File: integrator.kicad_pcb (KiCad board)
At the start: 4 copper layers, 65.5 x 117 mm, 97 parts, among them J1 SJ-3524-SMT, J2 SJ-3524-SMT, J5 USB4105-GF-A, J6 Conn_ARM_JTAG_SWD_10, J7 test point, SW1 EVQP40B3M, SW2 EVQP40B3M, SW3 EVQP40B3M, SW4 436333033816, U1 MCP1501T-30E_RW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

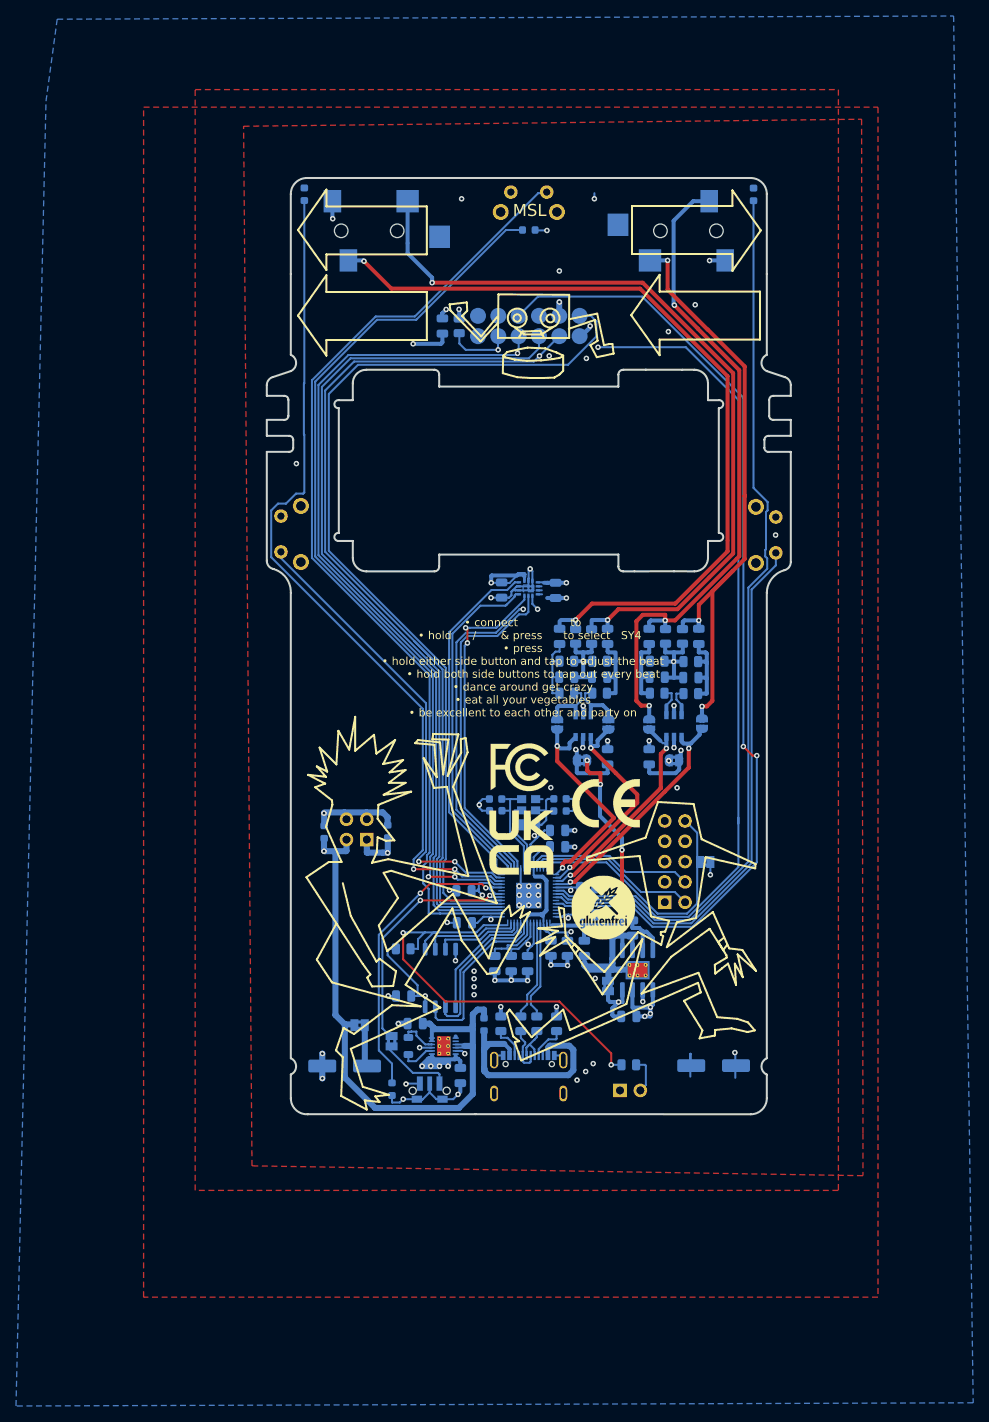
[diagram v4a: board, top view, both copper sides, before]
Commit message: adjusted jack positions, added back jumper
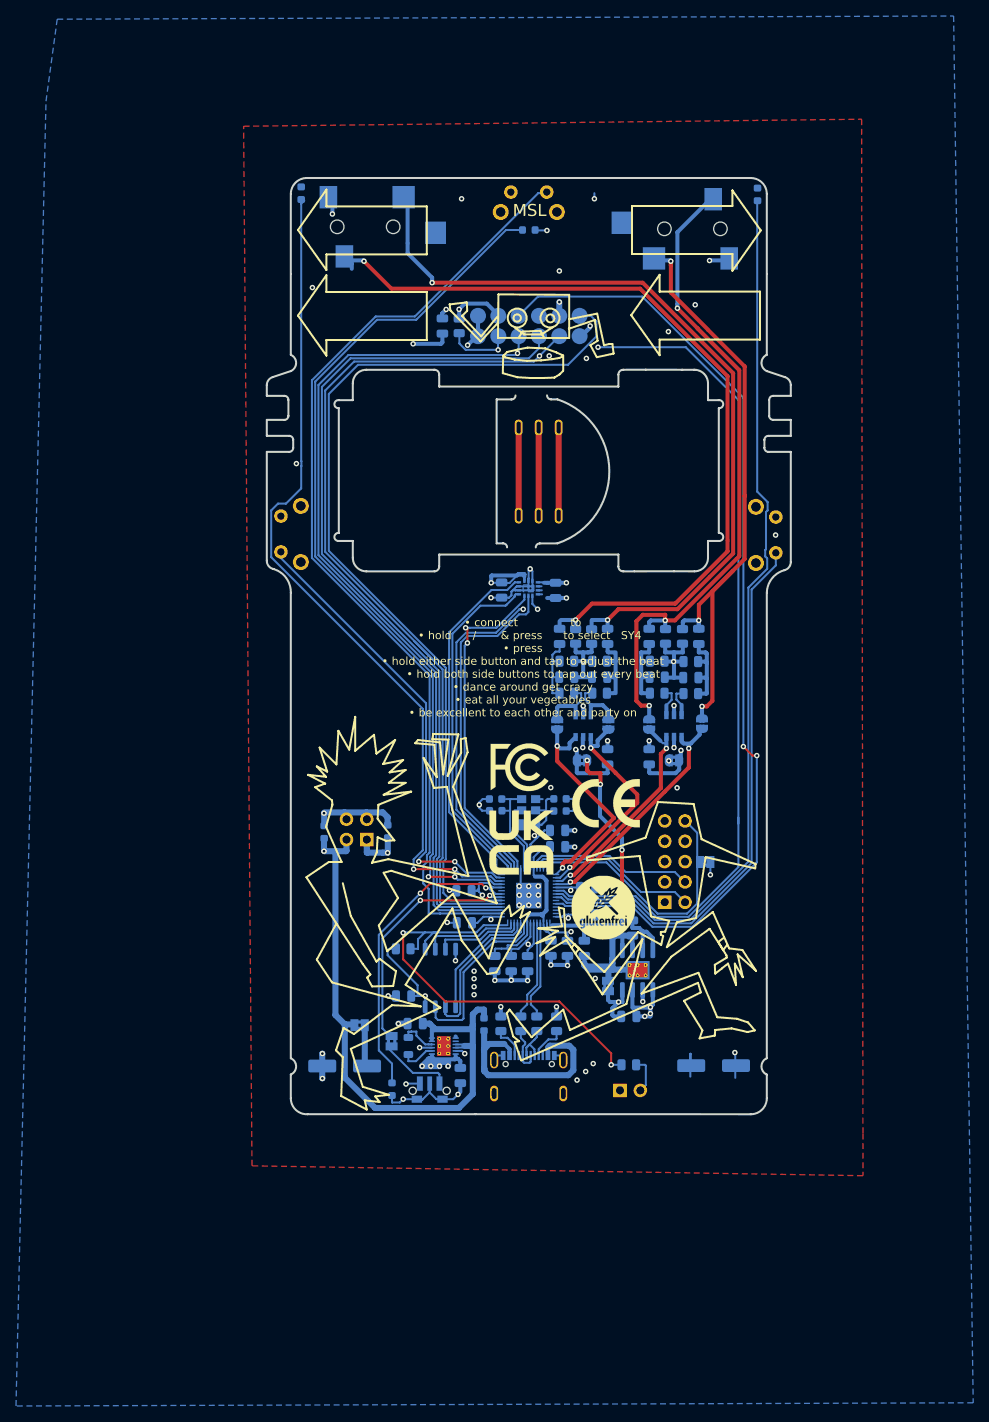
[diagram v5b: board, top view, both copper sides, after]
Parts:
- added J3: SP-3533-02, SP-3533-02:CUI_SP-3533-02, B.Cu at (155.3, 75.2)
- added J4: SP-3533-02, SP-3533-02:CUI_SP-3533-02, B.Cu at (155.3, 86.2)
- moved J1 0.71 mm to (130.1, 50.1)
- moved J2 0.56 mm to (178.0, 50.4)
- moved LED2 0.50 mm to (182.6, 46.0)
- moved LED1 0.41 mm to (125.6, 45.9)
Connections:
- POGO1 pad 1: Net-(POGO1-Pad1) -> Earth
- POGO1 pad 2: Net-(POGO1-Pad2) -> Earth
- POGO1 pad 4: Net-(POGO1-Pad4) -> /po_batt
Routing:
- net (no net): track 1.76 -> 35.1 mm
- net /po_batt: track 112.8 -> 118.7 mm
- net Earth: track 119.4 -> 123.6 mm, vias 56 -> 58
- net ring2_out: track 85.7 -> 84.2 mm
- net AGnd: track 55.1 -> 54.5 mm
- net led1: track 106.4 -> 105.8 mm
- removed copper zone on F.Cu, net Earth
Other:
- outline, holes or cut-outs redrawn

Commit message: widened edges to 60mm, re-added jumper
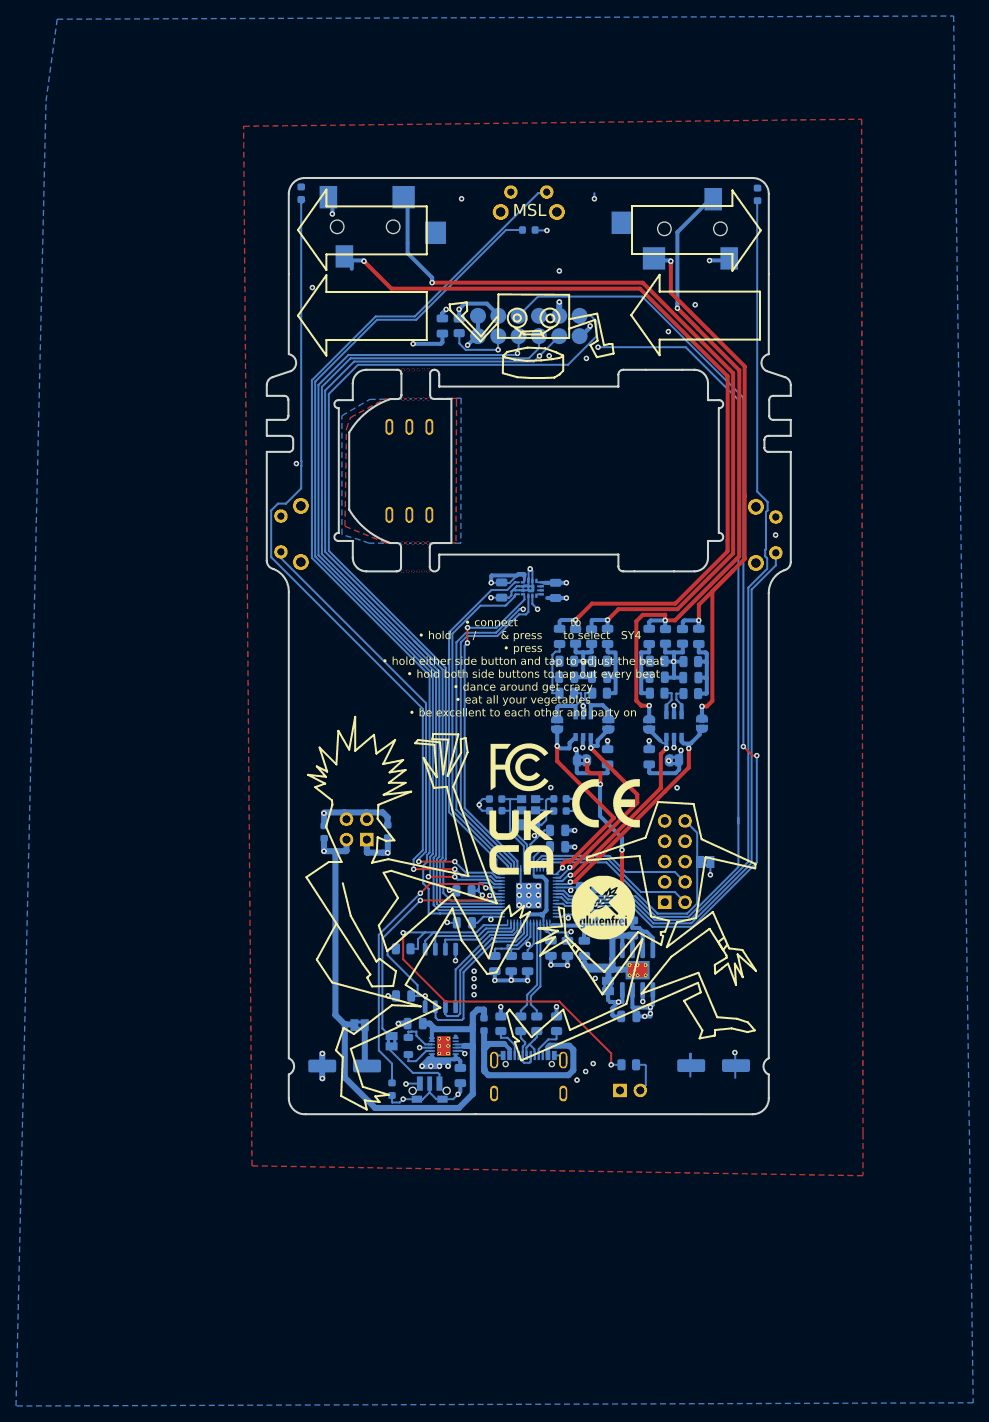
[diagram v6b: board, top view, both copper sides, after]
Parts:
- added REF**: mousebites_sparkfun, misc:mousebites_sparkfun, F.Cu at (137.7, 95.7)
- added REF**: mousebites_sparkfun, misc:mousebites_sparkfun, F.Cu at (137.6, 92.2)
- added REF**: mousebites_sparkfun, misc:mousebites_sparkfun, F.Cu at (142.2, 69.1)
- added REF**: mousebites_sparkfun, misc:mousebites_sparkfun, F.Cu at (142.1, 65.4)
- moved J4 19.6 mm to (139.1, 75.1), turned to 180 degrees
- moved J3 19.5 mm to (139.1, 86.1), turned to 180 degrees
- moved U3 0.50 mm to (154.5, 95.3)
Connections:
- C11 pad 1: /xin -> Net-(C11-Pad1)
- J3 pad 1: (no net) -> Net-(J3-Pad1)
- J3 pad 2: (no net) -> Net-(J3-Pad2)
- J3 pad 3: (no net) -> Net-(J3-Pad3)
- J4 pad 1: (no net) -> Net-(J3-Pad1)
- J4 pad 2: (no net) -> Net-(J3-Pad2)
- J4 pad 3: (no net) -> Earth
- POGO1 pad 1: Earth -> Net-(POGO1-Pad1)
- POGO1 pad 2: Earth -> Net-(POGO1-Pad2)
- POGO1 pad 4: /po_batt -> Net-(POGO1-Pad4)
- Y1 pad 2: (no net) -> Net-(C11-Pad1)
- Y1 pad 3: Net-(C11-Pad1) -> (no net)
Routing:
- net (no net): track 35.1 -> 12.0 mm
- net Net-(J3-Pad2): track 0.00 -> 11.1 mm
- net Net-(J3-Pad1): track 0.00 -> 11.1 mm
- net Net-(C11-Pad1): track 7.22 -> 8.10 mm
- added copper zone on F.Cu, net Earth
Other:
- outline, holes or cut-outs redrawn

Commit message: v8 schematic & pcb
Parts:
- removed the C11 at (149.9, 123.1)
- removed the C11 at (157.9, 121.6)
- removed the C11 at (157.9, 123.1)
- removed the C5 at (139.8, 149.7)
- removed D2: 450mv drop, Diode_SMD:D_0603_1608Metric
- removed the G*** at (163.4, 135.2)
- removed L1: 2.2uh, Inductor_SMD:L_0805_2012Metric
- added C11: 6pf, Capacitor_SMD:C_0603_1608Metric, B.Cu at (157.9, 123.1)
- added C35: 1uf ceramic, Capacitor_SMD:C_0805_2012Metric, B.Cu at (127.5, 128.8)
- added C36: TBD/DNC, Capacitor_SMD:C_0603_1608Metric, B.Cu at (149.9, 123.1)
- added C37: TBD/DNC, Capacitor_SMD:C_0603_1608Metric, B.Cu at (157.9, 121.6)
- added C9: 1uf ceramic, Capacitor_SMD:C_0805_2012Metric, B.Cu at (128.2, 121.7)
- added G***: LOGO, misc:glutenfree, F.Cu at (163.8, 135.6)
- C1: value 0.1uf -> 1uf ceramic
- C3: value 1nf -> 1uf ceramic
- C5: renamed from C9; value 10uf X5R -> 1uf ceramic
- D1: value <300mv drop -> <100mv drop; footprint Diode_SMD:D_0603_1608Metric -> Diode_SMD:D_SMB
- J6: footprint Connector_PinHeader_2.54mm:PinHeader_2x05_P2.54mm_Horizontal -> Connector_PinHeader_1.27mm:PinHeader_2x05_P1.27mm_Horizontal
- U1: value MCP1501T-30E_RW -> XC6415; footprint Package_SO:SOIC-8-1EP_3.9x4.9mm_P1.27mm_EP2.29x3mm_ThermalVias -> Package_TO_SOT_SMD:SOT-23-6_Handsoldering
- U2: value ISL9110 -> MCP1700-2302E/TT; footprint Package_DFN_QFN:TDFN-12-1EP_3x3mm_P0.4mm_EP1.70x2.45mm_ThermalVias -> Package_TO_SOT_SMD:SOT-23
- U4, U7: value NL27WZ16DTT1G -> TSOP6_1P70X3P10_ONS
- U6: value W25Q128JVS -> IS25WP128F-JBLE
- moved U2 31.5 mm to (127.5, 125.3), turned to 270 degrees
- moved C3 30.5 mm to (139.1, 150.1), turned to 90 degrees
- moved U1 27.4 mm to (141.9, 152.4)
- moved C1 21.3 mm to (145.5, 151.8), turned to 90 degrees
- moved JP10 10.2 mm to (177.5, 119.5), turned to 180 degrees
- moved D1 9.44 mm to (137.9, 125.5)
- moved J6 9.26 mm to (176.9, 127.4)
- moved JP6 2.69 mm to (166.6, 145.0), turned to 270 degrees
- moved C5 0.60 mm to (145.5, 156.8), turned to 90 degrees
- moved U3 0.50 mm to (154.0, 95.3)
- moved SW4 0.16 mm to (141.7, 157.9)
- moved LED4 0.16 mm to (137.0, 157.8)
- moved JP9 0.10 mm to (136.8, 151.9)
- moved C12 0.06 mm to (149.9, 121.6)
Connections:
- C3 pad 2: AGnd -> Earth
- C5 pad 1: VReg -> Earth
- C5 pad 2: Earth -> VRaw
- J3 pad 3: Net-(J3-Pad3) -> Earth
- J7 pad 1: VReg -> VRaw
- JP11 pad 1: Net-(C15-Pad1) -> VRaw
- JP11 pad 2: VRaw -> Net-(C15-Pad1)
- JP6 pad 1: Earth -> AGnd
- JP6 pad 2: AGnd -> Earth
- POGO1 pad 1: Net-(POGO1-Pad1) -> Earth
- POGO1 pad 2: Net-(POGO1-Pad2) -> Earth
- POGO1 pad 4: Net-(POGO1-Pad4) -> /po_batt
- U1 pad 1: VReg -> VRaw
- U1 pad 2: Earth -> VRaw
- U1 pad 3: VReg -> Aref_enable
- U1 pad 4: Earth -> VAref
- U1 pad 5: AGnd -> Earth
- U1 pad 6: AGnd -> VReg
- U2 pad 1: VReg -> Earth
- U2 pad 2: Net-(L1-Pad1) -> /po_batt
- U2 pad 3: Earth -> VRaw
- U5 pad 39: Net-(U5-Pad39) -> Aref_enable
- Y1 pad 2: Net-(C11-Pad1) -> Earth
- Y1 pad 3: (no net) -> Net-(C11-Pad1)
- Y1 pad 4: (no net) -> Earth
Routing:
- net VReg: track 274.5 -> 204.0 mm, vias 25 -> 18
- net VAref: track 54.5 -> 97.7 mm, vias 5 -> 18
- net Aref_enable: track 0.00 -> 36.1 mm, vias 0 -> 2
- net Earth: track 123.6 -> 150.0 mm, vias 58 -> 72
- net VRaw: track 79.3 -> 97.0 mm, vias 1 -> 0
- net AGnd: track 54.5 -> 37.1 mm, vias 6 -> 7
- net Net-(JP10-Pad2): track 63.4 -> 76.6 mm
- net (no net): track 12.0 -> 0.00 mm
- net pi_swclk: track 21.0 -> 29.2 mm, vias 0 -> 2
- net /po_batt: track 118.7 -> 124.0 mm
- net pi_swdio: track 21.3 -> 26.1 mm
- net Net-(L1-Pad2): track 4.62 -> 0.00 mm
- net Net-(L1-Pad1): track 4.31 -> 0.00 mm
- net ring1: track 27.7 -> 24.4 mm
- net po_reset: track 127.0 -> 124.2 mm
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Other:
- board text added: "!!"
- board text added: "+"
- board text added: "-"
- board text added: ">"
- board text added: "JLCJLCJLCJLC"
- board text added: "O"
- board text added: "USB C"
- board text added: "`"
- board text added: "v"
- board text added: "|"
- board text added: "»"
- board text removed: "C"

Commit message: reorg po debug pins
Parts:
- U4, U7: value TSOP6_1P70X3P10_ONS -> NL27WZ16DTT1G
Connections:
- U5 pad 2: sw3 -> po_swo
- U5 pad 3: po_swclk -> sw3
- U5 pad 4: po_swdio -> po_swclk
- U5 pad 5: po_swo -> po_swdio
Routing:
- net sw3: track 120.7 -> 121.9 mm, vias 0 -> 2
- net po_swdio: track 109.7 -> 109.1 mm
- net po_swclk: track 108.7 -> 108.2 mm
- net po_swo: track 113.7 -> 114.2 mm, vias 1 -> 3
